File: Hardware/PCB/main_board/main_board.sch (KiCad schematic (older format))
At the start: 0 parts

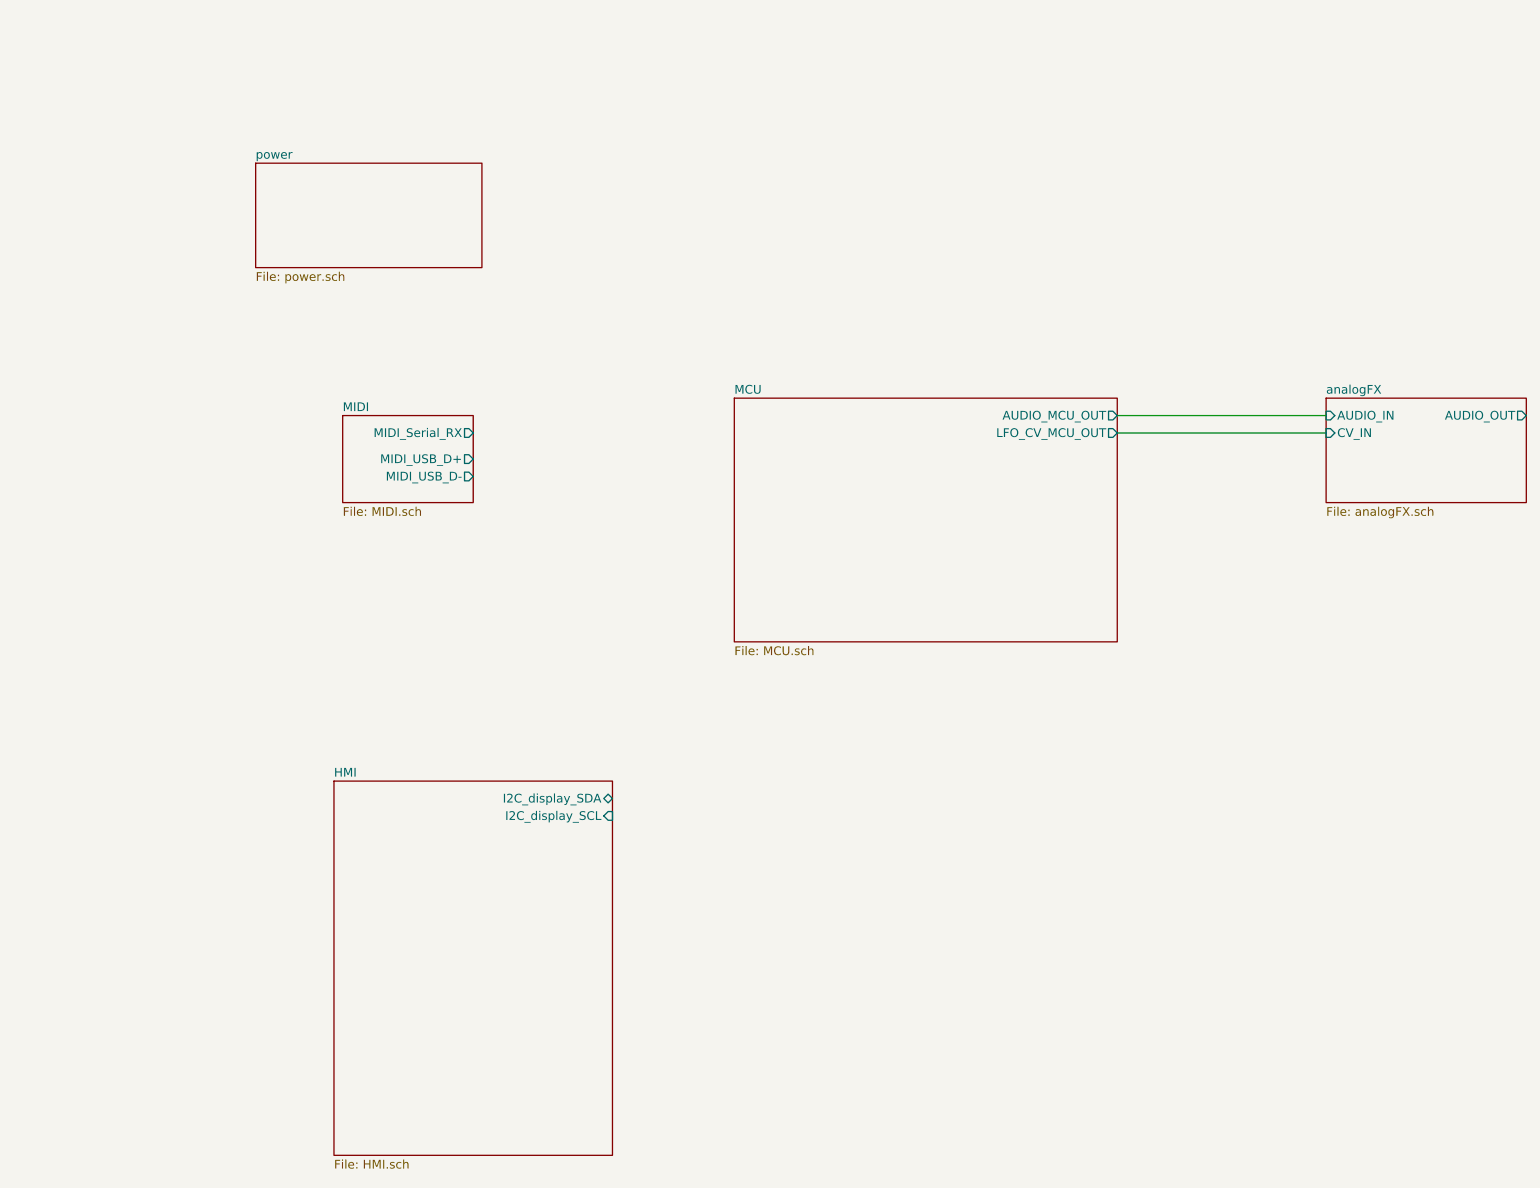
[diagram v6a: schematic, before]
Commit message: Add HMI buttons and pots to PCB
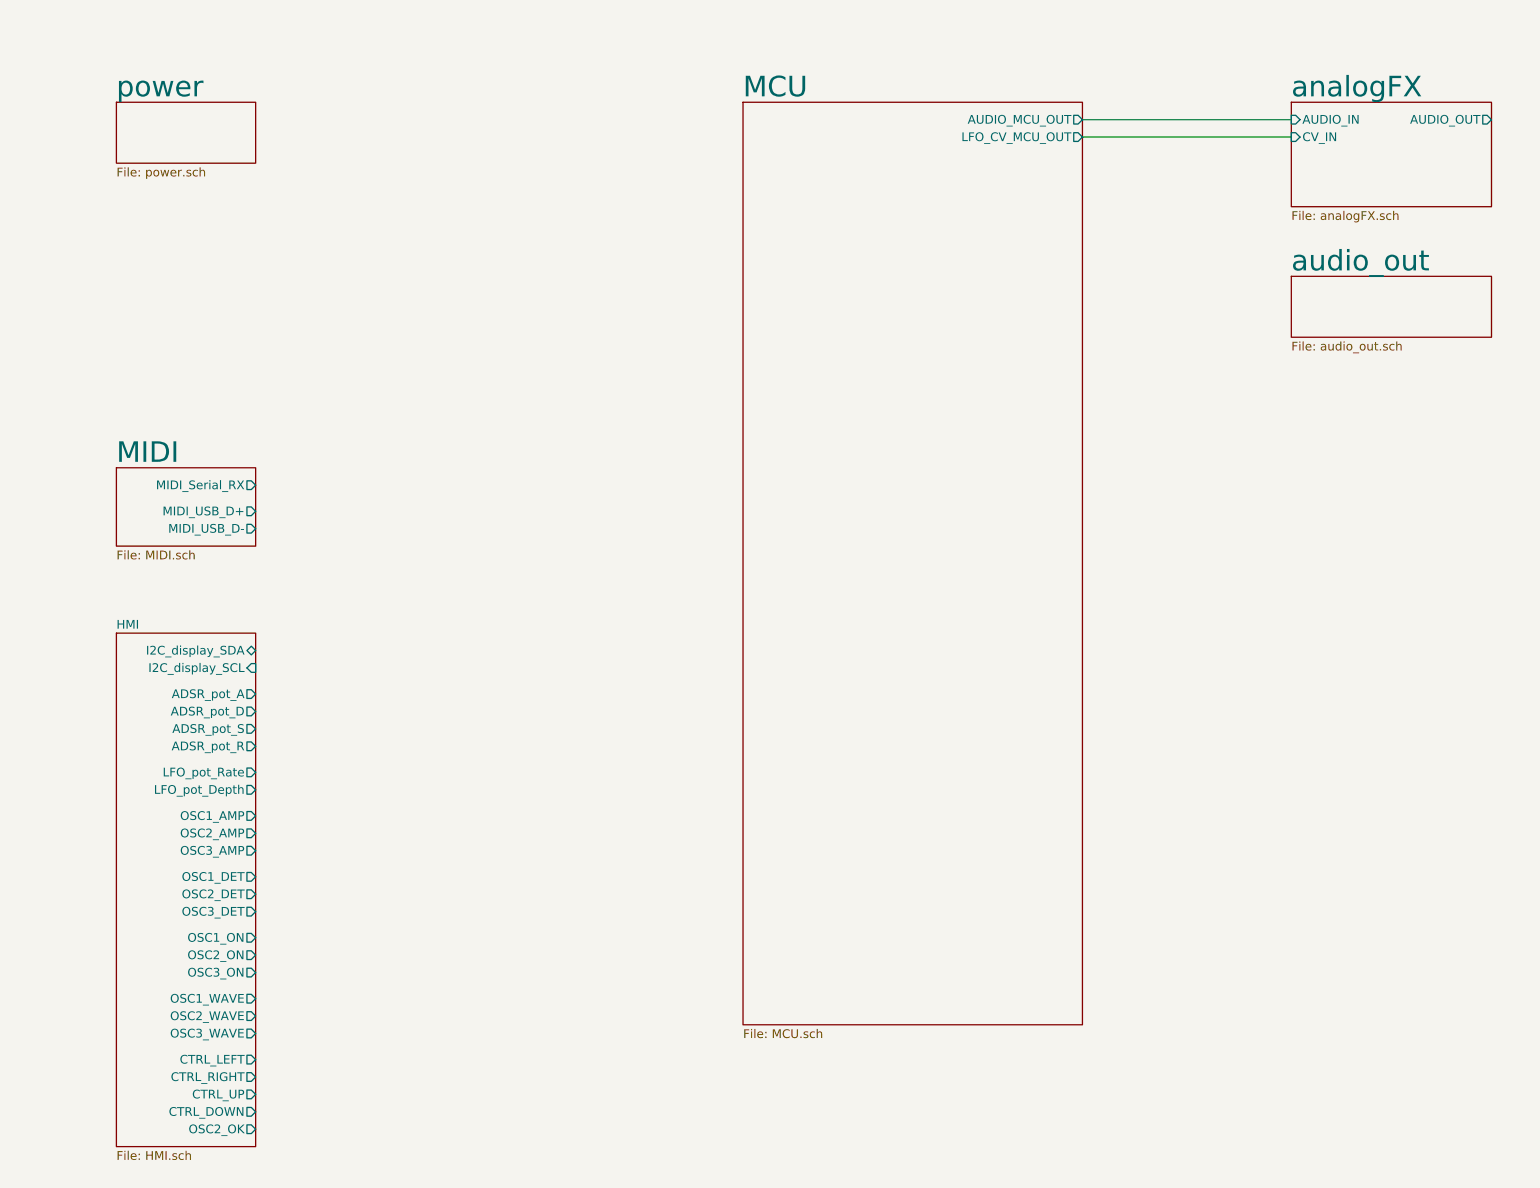
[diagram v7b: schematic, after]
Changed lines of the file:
@@
 $Descr A4 11693 8268
 encoding utf-8
-Sheet 1 6
+Sheet 1 7
 Title ""
 Date ""
@@
 $EndDescr
 Wire Wire Line
-	6950 2950 8150 2950
+	6750 1250 7950 1250
 Wire Wire Line
-	6950 3050 8150 3050
+	6750 1350 7950 1350
 $Sheet
-S 2500 2950 750  500
+S 1200 3250 800  450
 U 5E513BF6
-F0 "MIDI" 50
+F0 "MIDI" 118
 F1 "MIDI.sch" 50
-F2 "MIDI_Serial_RX" O R 3250 3050 50
-F3 "MIDI_USB_D+" O R 3250 3200 50
-F4 "MIDI_USB_D-" O R 3250 3300 50
+F2 "MIDI_Serial_RX" O R 2000 3350 50
+F3 "MIDI_USB_D+" O R 2000 3500 50
+F4 "MIDI_USB_D-" O R 2000 3600 50
 $EndSheet
 $Sheet
-S 8150 2850 1150 600
-U 5E632F77
-F0 "analogFX" 50
-F1 "analogFX.sch" 50
-F2 "AUDIO_OUT" O R 9300 2950 50
-F3 "CV_IN" I L 8150 3050 50
-F4 "AUDIO_IN" I L 8150 2950 50
+S 4800 1150 1950 5300
+U 5E658709
+F0 "MCU" 118
+F1 "MCU.sch" 50
+F2 "AUDIO_MCU_OUT" O R 6750 1250 50
+F3 "LFO_CV_MCU_OUT" O R 6750 1350 50
 $EndSheet
 $Sheet
-S 4750 2850 2200 1400
-U 5E658709
-F0 "MCU" 50
-F1 "MCU.sch" 50
-F2 "AUDIO_MCU_OUT" O R 6950 2950 50
-F3 "LFO_CV_MCU_OUT" O R 6950 3050 50
-$EndSheet
-$Sheet
-S 2000 1500 1300 600
+S 1200 1150 800  350
 U 5E57C92D
-F0 "power" 50
+F0 "power" 118
 F1 "power.sch" 50
 $EndSheet
 $Sheet
-S 2450 5050 1600 2150
+S 7950 2150 1150 350
+U 5E68385C
+F0 "audio_out" 118
+F1 "audio_out.sch" 50
+$EndSheet
+$Sheet
+S 7950 1150 1150 600
+U 5E632F77
+F0 "analogFX" 118
+F1 "analogFX.sch" 50
+F2 "AUDIO_OUT" O R 9100 1250 50
+F3 "CV_IN" I L 7950 1350 50
+F4 "AUDIO_IN" I L 7950 1250 50
+$EndSheet
+$Sheet
+S 1200 4200 800  2950
 U 5E525BAF
 F0 "HMI" 50
 F1 "HMI.sch" 50
-F2 "I2C_display_SDA" B R 4050 5150 50
-F3 "I2C_display_SCL" I R 4050 5250 50
+F2 "I2C_display_SDA" B R 2000 4300 50
+F3 "I2C_display_SCL" I R 2000 4400 50
+F4 "ADSR_pot_A" O R 2000 4550 50
+F5 "ADSR_pot_D" O R 2000 4650 50
+F6 "ADSR_pot_S" O R 2000 4750 50
+F7 "ADSR_pot_R" O R 2000 4850 50
+F8 "LFO_pot_Rate" O R 2000 5000 50
+F9 "LFO_pot_Depth" O R 2000 5100 50
+F10 "OSC1_AMP" O R 2000 5250 50
+F11 "OSC2_AMP" O R 2000 5350 50
+F12 "OSC3_AMP" O R 2000 5450 50
+F13 "OSC1_DET" O R 2000 5600 50
+F14 "OSC2_DET" O R 2000 5700 50
+F15 "OSC3_DET" O R 2000 5800 50
+F16 "OSC1_ON" O R 2000 5950 50
+F17 "OSC2_ON" O R 2000 6050 50
+F18 "OSC3_ON" O R 2000 6150 50
+F19 "OSC1_WAVE" O R 2000 6300 50
+F20 "OSC2_WAVE" O R 2000 6400 50
+F21 "OSC3_WAVE" O R 2000 6500 50
+F22 "CTRL_LEFT" O R 2000 6650 50
+F23 "CTRL_RIGHT" O R 2000 6750 50
+F24 "CTRL_UP" O R 2000 6850 50
+F25 "CTRL_DOWN" O R 2000 6950 50
+F26 "OSC2_OK" O R 2000 7050 50
 $EndSheet
 $EndSCHEMATC

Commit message: Place HMI
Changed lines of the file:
@@
 F6 "ADSR_pot_S" O R 2000 4750 50
 F7 "ADSR_pot_R" O R 2000 4850 50
-F8 "LFO_pot_Rate" O R 2000 5000 50
-F9 "LFO_pot_Depth" O R 2000 5100 50
-F10 "OSC1_AMP" O R 2000 5250 50
-F11 "OSC2_AMP" O R 2000 5350 50
-F12 "OSC3_AMP" O R 2000 5450 50
-F13 "OSC1_DET" O R 2000 5600 50
-F14 "OSC2_DET" O R 2000 5700 50
-F15 "OSC3_DET" O R 2000 5800 50
-F16 "OSC1_ON" O R 2000 5950 50
-F17 "OSC2_ON" O R 2000 6050 50
-F18 "OSC3_ON" O R 2000 6150 50
-F19 "OSC1_WAVE" O R 2000 6300 50
-F20 "OSC2_WAVE" O R 2000 6400 50
-F21 "OSC3_WAVE" O R 2000 6500 50
-F22 "CTRL_LEFT" O R 2000 6650 50
-F23 "CTRL_RIGHT" O R 2000 6750 50
-F24 "CTRL_UP" O R 2000 6850 50
-F25 "CTRL_DOWN" O R 2000 6950 50
-F26 "OSC2_OK" O R 2000 7050 50
+F8 "OSC1_AMP" O R 2000 5250 50
+F9 "OSC2_AMP" O R 2000 5350 50
+F10 "OSC3_AMP" O R 2000 5450 50
+F11 "OSC1_DET" O R 2000 5600 50
+F12 "OSC2_DET" O R 2000 5700 50
+F13 "OSC3_DET" O R 2000 5800 50
+F14 "OSC1_ON" O R 2000 5950 50
+F15 "OSC2_ON" O R 2000 6050 50
+F16 "OSC3_ON" O R 2000 6150 50
+F17 "OSC1_WAVE" O R 2000 6300 50
+F18 "OSC2_WAVE" O R 2000 6400 50
+F19 "OSC3_WAVE" O R 2000 6500 50
+F20 "CTRL_LEFT" O R 2000 6650 50
+F21 "CTRL_RIGHT" O R 2000 6750 50
+F22 "CTRL_UP" O R 2000 6850 50
+F23 "CTRL_DOWN" O R 2000 6950 50
+F24 "OSC2_OK" O R 2000 7050 50
+F25 "LFO_pot_RATE" O R 2000 5000 50
+F26 "LFO_pot_DEPTH" O R 2000 5100 50
 $EndSheet
 $EndSCHEMATC
